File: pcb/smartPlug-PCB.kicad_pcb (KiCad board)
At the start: 2 copper layers, 91 x 71.5 mm, 14 parts, among them J1 Screw_Terminal_01x02, J2 Screw_Terminal_01x02, K1 SRD-05VDC-SL-C, Q1 2N3904, SW2 SW_Push, U1 ESP32-C3_SUPERMINI_TH, U2 HLK-PM01

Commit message: Added relay toggling, tested. Added a missing ground trace to PCB, regenereated gerbers.
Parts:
- J1: value Screw_Terminal_01x02 -> Screw_Terminal_01x02-MainIn
- J2: value Screw_Terminal_01x02 -> Screw_Terminal_01x02-MainOut
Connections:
- U1 pad G: Net-(U1-GND) -> GND
- U2 pad 3: Net-(U1-GND) -> GND
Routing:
- net GND: track 26.0 -> 109.8 mm, vias 0 -> 2
- net Net-(U1-GND): track 49.2 -> 0.00 mm, vias 2 -> 0
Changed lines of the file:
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@@
 			)
 		)
-		(property "Value" "Screw_Terminal_01x02"
+		(property "Value" "Screw_Terminal_01x02-MainOut"
 			(at 2.54 5.72 90)
 			(layer "F.Fab")
@@
 			(layers "*.Cu" "*.Mask")
 			(remove_unused_layers no)
-			(net "Net-(U1-GND)")
+			(net "GND")
 			(pinfunction "GND_G")
 			(pintype "power_in")
@@
 			)
 		)
-		(property "Value" "Screw_Terminal_01x02"
+		(property "Value" "Screw_Terminal_01x02-MainIn"
 			(at 2.54 5.72 90)
 			(layer "F.Fab")
@@
 			(layers "*.Cu" "*.Mask")
 			(remove_unused_layers no)
-			(net "Net-(U1-GND)")
+			(net "GND")
 			(pinfunction "-Vout_3")
 			(pintype "power_out")
@@
 	)
 	(segment
+		(start 86.14 74.88)
+		(end 95.02 66)
+		(width 0.2)
+		(layer "F.Cu")
+		(net "GND")
+	)
+	(segment
+		(start 111.0925 64.4)
+		(end 124.2925 51.2)
+		(width 0.2)
+		(layer "F.Cu")
+		(net "GND")
+	)
+	(segment
+		(start 124.2925 51.2)
+		(end 124.2925 50)
+		(width 0.2)
+		(layer "F.Cu")
+		(net "GND")
+	)
+	(segment
 		(start 131.23 76.36)
 		(end 128.495 79.095)
@@
 	)
 	(segment
+		(start 107.5 64.4)
+		(end 111.0925 64.4)
+		(width 0.2)
+		(layer "F.Cu")
+		(net "GND")
+	)
+	(segment
 		(start 128.495 85.5)
 		(end 130.995 88)
@@
 	)
 	(segment
+		(start 95.02 66)
+		(end 106 66)
+		(width 0.2)
+		(layer "F.Cu")
+		(net "GND")
+	)
+	(via
+		(at 107.5 64.4)
+		(size 0.6)
+		(drill 0.3)
+		(layers "F.Cu" "B.Cu")
+		(net "GND")
+	)
+	(via
+		(at 106 66)
+		(size 0.6)
+		(drill 0.3)
+		(layers "F.Cu" "B.Cu")
+		(net "GND")
+	)
+	(segment
+		(start 107.5 64.5)
+		(end 107.5 64.4)
+		(width 0.2)
+		(layer "B.Cu")
+		(net "GND")
+	)
+	(segment
+		(start 116.27 85.5)
+		(end 96.76 85.5)
+		(width 0.2)
+		(layer "B.Cu")
+		(net "GND")
+	)
+	(segment
+		(start 96.76 85.5)
+		(end 86.14 74.88)
+		(width 0.2)
+		(layer "B.Cu")
+		(net "GND")
+	)
+	(segment
+		(start 106 66)
+		(end 107.5 64.5)
+		(width 0.2)
+		(layer "B.Cu")
+		(net "GND")
+	)
+	(segment
 		(start 110.96 87)
 		(end 127.595 87)
@@
 	)
 	(segment
-		(start 86.14 74.88)
-		(end 95.02 66)
-		(width 0.2)
-		(layer "F.Cu")
-		(net "Net-(U1-GND)")
-	)
-	(segment
-		(start 111.0925 64.4)
-		(end 124.2925 51.2)
-		(width 0.2)
-		(layer "F.Cu")
-		(net "Net-(U1-GND)")
-	)
-	(segment
-		(start 124.2925 51.2)
-		(end 124.2925 50)
-		(width 0.2)
-		(layer "F.Cu")
-		(net "Net-(U1-GND)")
-	)
-	(segment
-		(start 107.5 64.4)
-		(end 111.0925 64.4)
-		(width 0.2)
-		(layer "F.Cu")
-		(net "Net-(U1-GND)")
-	)
-	(segment
-		(start 95.02 66)
-		(end 106 66)
-		(width 0.2)
-		(layer "F.Cu")
-		(net "Net-(U1-GND)")
-	)
-	(via
-		(at 107.5 64.4)
-		(size 0.6)
-		(drill 0.3)
-		(layers "F.Cu" "B.Cu")
-		(net "Net-(U1-GND)")
-	)
-	(via
-		(at 106 66)
-		(size 0.6)
-		(drill 0.3)
-		(layers "F.Cu" "B.Cu")
-		(net "Net-(U1-GND)")
-	)
-	(segment
-		(start 107.5 64.5)
-		(end 107.5 64.4)
-		(width 0.2)
-		(layer "B.Cu")
-		(net "Net-(U1-GND)")
-	)
-	(segment
-		(start 106 66)
-		(end 107.5 64.5)
-		(width 0.2)
-		(layer "B.Cu")
-		(net "Net-(U1-GND)")
-	)
-	(segment

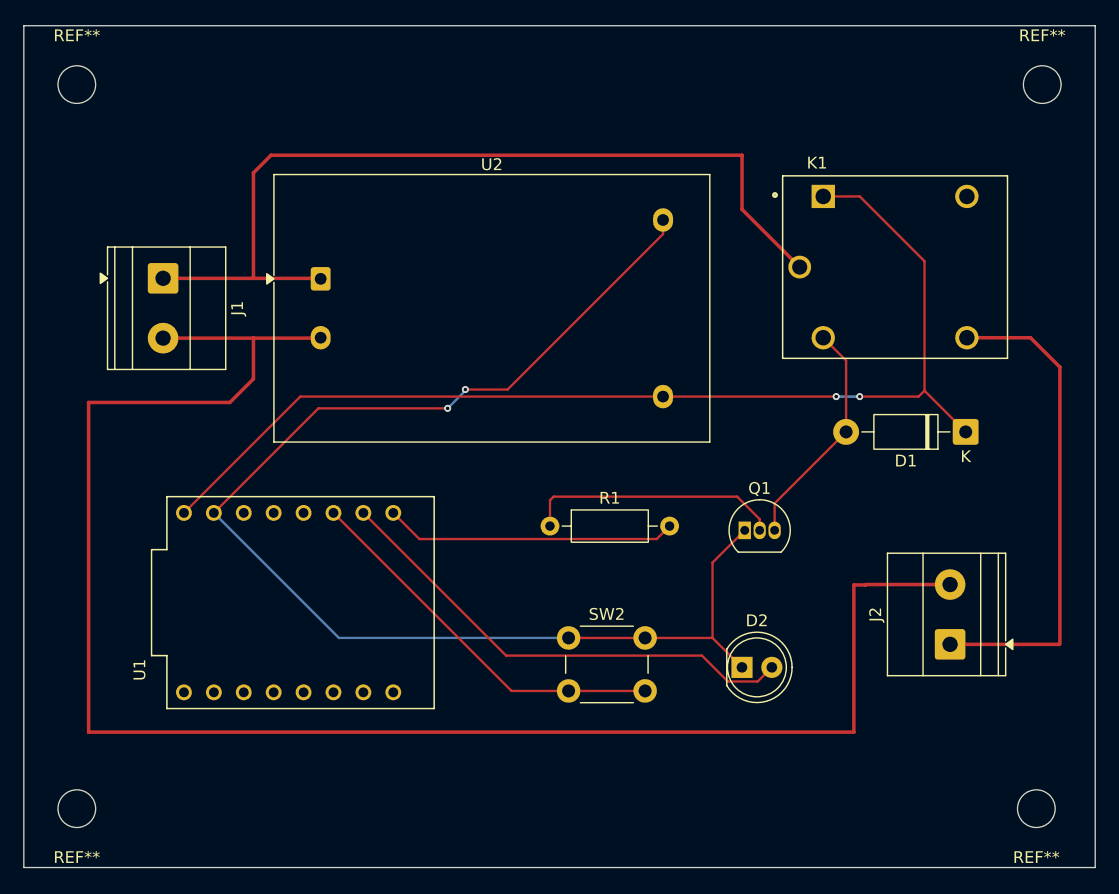
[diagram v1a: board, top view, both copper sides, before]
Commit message: Respun PCB. Replaced LED with onboard LED in FW.
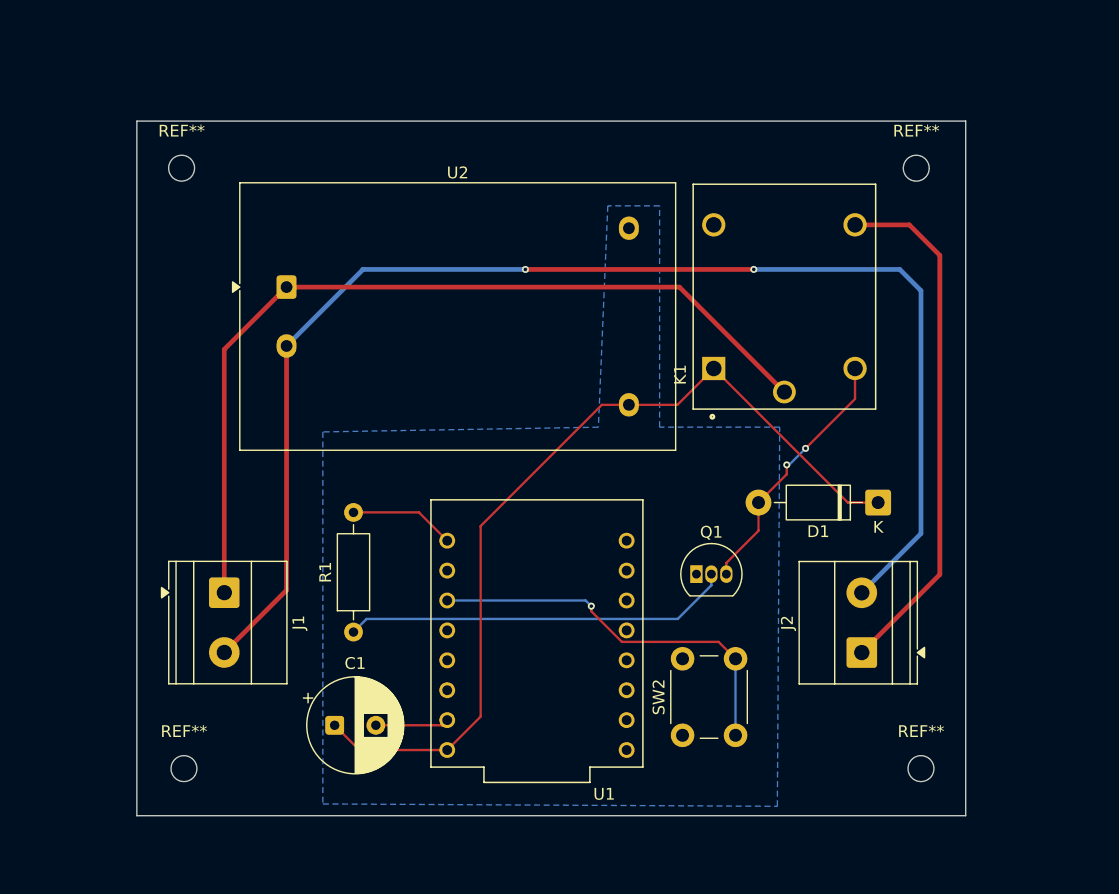
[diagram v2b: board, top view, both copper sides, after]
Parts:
- removed D2: LED, LED_THT:LED_D5.0mm
- removed the REF** at (74.5, 100.0)
- removed the REF** at (156.0, 100.0)
- removed the REF** at (74.5, 38.5)
- removed the REF** at (156.5, 38.5)
- added C1: 470u, Capacitor_THT:CP_Radial_D8.0mm_P3.50mm, F.Cu at (96.4, 92.9)
- added REF**: MountingHole_2.2mm_M2, MountingHole:MountingHole_2.2mm_M2, F.Cu at (83.6, 96.6)
- added REF**: MountingHole_2.2mm_M2, MountingHole:MountingHole_2.2mm_M2, F.Cu at (145.8, 45.6)
- added REF**: MountingHole_2.2mm_M2, MountingHole:MountingHole_2.2mm_M2, F.Cu at (83.4, 45.6)
- added REF**: MountingHole_2.2mm_M2, MountingHole:MountingHole_2.2mm_M2, F.Cu at (146.2, 96.6)
- moved J1 27.2 mm to (87.0, 81.7)
- moved U1 20.3 mm to (113.6, 85.1), turned to 180 degrees
- moved R1 19.0 mm to (98.0, 85.0), turned to 90 degrees
- moved SW2 12.7 mm to (126.0, 93.8), turned to 90 degrees
- moved K1 9.73 mm to (134.6, 56.5), turned to 90 degrees
- moved D1 9.56 mm to (142.6, 74.0)
- moved J2 7.53 mm to (141.2, 86.7)
- moved Q1 5.54 mm to (127.1, 80.1)
- moved U2 2.98 mm to (92.3, 55.7)
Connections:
- U1 pad 1: Net-(D2-A) -> unconnected-(U1-GPIO1-Pad1)
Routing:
- net GND: track 109.8 -> 6.24 mm, vias 2 -> 0
- net Net-(D2-A): track 41.1 -> 0.00 mm
- net Net-(J1-Pin_2): track 145.4 -> 113.3 mm, vias 0 -> 2
- net Net-(D1-K): track 94.0 -> 74.6 mm, vias 2 -> 0
- net Net-(U1-GPIO0): track 24.8 -> 8.95 mm
- net Net-(Q1-B): track 21.9 -> 33.0 mm
- net Net-(J2-Pin_1): track 41.8 -> 44.8 mm
- net Net-(D1-A): track 19.7 -> 22.1 mm, vias 0 -> 2
- net Net-(J1-Pin_1): track 76.0 -> 74.1 mm
- net Net-(U1-GPIO2): track 32.7 -> 33.3 mm, vias 0 -> 1
- added copper zone on B.Cu, net GND
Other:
- board size 91 x 71.5 mm -> 70.4 x 59 mm
